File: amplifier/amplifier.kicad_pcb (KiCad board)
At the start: 2 copper layers, 54 x 46.8 mm, 20 parts, among them J1 INPUT, J3 POWER IN, Q1 TIP41, Q2 TIP42, U1 LM833

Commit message: Added HP@DESKTOP-614QREO MINGW64 ~/Documents/KICAD Project (main) $
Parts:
- J2: renamed from SPK OUT
- moved . 1.77 mm to (95.2, 79.5)
- moved . 1.77 mm to (46.8, 79.2)
- moved . 0.79 mm to (95.0, 119.5)
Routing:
- net Net-(D1-K): track 70.9 -> 46.9 mm
- net Net-(J2-Pin_2): track 99.6 -> 100.1 mm
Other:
- board size 54 x 46.8 mm -> 56.7 x 49.5 mm
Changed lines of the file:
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@@
 		(sheetname "/")
 		(sheetfile "amplifier.kicad_sch")
+		(units
+			(unit
+				(name "A")
+				(pins "1" "2")
+			)
+		)
 		(attr through_hole)
 		(duplicate_pad_numbers_are_jumpers no)
@@
 	(footprint "MountingHole:MountingHole_2.2mm_M2_Pad"
 		(layer "F.Cu")
-		(at 95 81.25)
+		(at 95.25 79.5)
 		(descr "Mounting Hole 2.2mm, M2, generated by kicad-footprint-generator mountinghole.py")
 		(tags "mountinghole M2")
@@
 			(at 0 -3.15 0)
 			(layer "B.Cu")
+			(hide yes)
 			(effects
 				(font
@@
 		(sheetname "/")
 		(sheetfile "amplifier.kicad_sch")
+		(units
+			(unit
+				(name "A")
+				(pins "1" "2")
+			)
+		)
 		(attr through_hole)
 		(duplicate_pad_numbers_are_jumpers no)
@@
 			)
 		)
-		(property "Description" ""
+		(property "Description" "Trim-potentiometer, US symbol"
 			(at 0 0 0)
 			(layer "F.Fab")
@@
 		(sheetname "/")
 		(sheetfile "amplifier.kicad_sch")
+		(units
+			(unit
+				(name "A")
+				(pins "1" "3" "2")
+			)
+		)
 		(attr through_hole)
 		(duplicate_pad_numbers_are_jumpers no)
@@
 		(descr "Terminal block Altech AK300, 45Degree (cable under 45degree), 2 pins, pitch 5mm, size 10x12.5mm, drill diameter 1.3mm, pad diameter 3mm, https://www.altechcorp.com/PDFS/PCBMETRC.PDF#page=5, generated with kicad-footprint-generator TerminalBlock_Altech")
 		(tags "THT Terminal block Altech AK300 45Degree pitch 5mm size 10x12.5mm drill 1.3mm pad 3mm")
-		(property "Reference" "SPK OUT"
+		(property "Reference" "J2"
 			(at 2.5 9.5 0)
 			(layer "F.SilkS")
@@
 		(sheetname "/")
 		(sheetfile "amplifier.kicad_sch")
+		(units
+			(unit
+				(name "A")
+				(pins "1" "2")
+			)
+		)
 		(attr through_hole)
 		(duplicate_pad_numbers_are_jumpers no)
@@
 		(sheetname "/")
 		(sheetfile "amplifier.kicad_sch")
+		(units
+			(unit
+				(name "A")
+				(pins "1" "2")
+			)
+		)
 		(attr through_hole)
 		(duplicate_pad_numbers_are_jumpers no)
@@
 		(sheetname "/")
 		(sheetfile "amplifier.kicad_sch")
+		(units
+			(unit
+				(name "A")
+				(pins "1" "2" "3")
+			)
+		)
 		(attr through_hole)
 		(duplicate_pad_numbers_are_jumpers no)
@@
 			(at 0 -3.15 0)
 			(layer "B.Cu")
+			(hide yes)
 			(effects
 				(font
@@
 		(sheetname "/")
 		(sheetfile "amplifier.kicad_sch")
+		(units
+			(unit
+				(name "A")
+				(pins "1" "2")
+			)
+		)
 		(attr through_hole)
 		(duplicate_pad_numbers_are_jumpers no)
@@
 		(sheetname "/")
 		(sheetfile "amplifier.kicad_sch")
+		(units
+			(unit
+				(name "A")
+				(pins "1" "2" "3")
+			)
+		)
 		(attr through_hole)
 		(duplicate_pad_numbers_are_jumpers no)
@@
 	(footprint "MountingHole:MountingHole_2.2mm_M2_Pad"
 		(layer "F.Cu")
-		(at 46.5 81)
+		(at 46.75 79.25)
 		(descr "Mounting Hole 2.2mm, M2, generated by kicad-footprint-generator mountinghole.py")
 		(tags "mountinghole M2")
@@
 			(at 0 -3.15 0)
 			(layer "B.Cu")
+			(hide yes)
 			(effects
 				(font
@@
 	(footprint "MountingHole:MountingHole_2.2mm_M2_Pad"
 		(layer "F.Cu")
-		(at 94.75 120.25)
+		(at 95 119.5)
 		(descr "Mounting Hole 2.2mm, M2, generated by kicad-footprint-generator mountinghole.py")
 		(tags "mountinghole M2")
@@
 			(at 0 -3.15 0)
 			(layer "B.Cu")
+			(hide yes)
 			(effects
 				(font
@@
 		(sheetname "/")
 		(sheetfile "amplifier.kicad_sch")
+		(units
+			(unit
+				(name "A")
+				(pins "1" "2")
+			)
+		)
 		(attr through_hole)
 		(duplicate_pad_numbers_are_jumpers no)
@@
 		(tags "TO-220-3 Vertical RM 2.54mm")
 		(property "Reference" "Q2"
-			(at 2.54 -4.1 90)
+			(at 3 -4.5 90)
 			(layer "F.SilkS")
 			(effects
@@
 		(sheetname "/")
 		(sheetfile "amplifier.kicad_sch")
+		(units
+			(unit
+				(name "A")
+				(pins "1" "2" "3")
+			)
+		)
 		(attr through_hole)
 		(duplicate_pad_numbers_are_jumpers no)
@@
 		(sheetname "/")
 		(sheetfile "amplifier.kicad_sch")
+		(units
+			(unit
+				(name "A")
+				(pins "1" "2")
+			)
+		)
 		(attr through_hole)
 		(duplicate_pad_numbers_are_jumpers no)
@@
 		(sheetname "/")
 		(sheetfile "amplifier.kicad_sch")
+		(units
+			(unit
+				(name "A")
+				(pins "3" "2" "1")
+			)
+			(unit
+				(name "B")
+				(pins "5" "6" "7")
+			)
+			(unit
+				(name "C")
+				(pins "8" "4")
+			)
+		)
 		(attr through_hole)
 		(duplicate_pad_numbers_are_jumpers no)
@@
 		(sheetname "/")
 		(sheetfile "amplifier.kicad_sch")
+		(units
+			(unit
+				(name "A")
+				(pins "1" "2")
+			)
+		)
 		(attr through_hole)
 		(duplicate_pad_numbers_are_jumpers no)
@@
 	)
 	(gr_rect
-		(start 44 76.25)
-		(end 98 123)
+		(start 43.25 75.553072)
+		(end 99.999999 125.089914)
 		(stroke
 			(width 0.05)
@@
 	)
 	(segment
-		(start 56.5 120)
-		(end 53.5 117)
-		(width 1)
+		(start 86.9 110.390173)
+		(end 86.9 101.14)
+		(width 1.2)
 		(layer "F.Cu")
 		(net "Net-(J2-Pin_2)")
 	)
 	(segment
-		(start 89 99.04)
-		(end 83.29 99.04)
-		(width 0.5)
+		(start 83.29 99.04)
+		(end 89 99.04)
+		(width 1.2)
 		(layer "F.Cu")
 		(net "Net-(J2-Pin_2)")
 	)
 	(segment
-		(start 83.29 99.04)
-		(end 82.5 98.25)
-		(width 0.5)
+		(start 86.9 101.14)
+		(end 87.25 100.79)
+		(width 1.2)
 		(layer "F.Cu")
 		(net "Net-(J2-Pin_2)")
 	)
 	(segment
-		(start 68.75 120)
-		(end 56.5 120)
-		(width 1)
+		(start 82.5 98.25)
+		(end 83.29 99.04)
+		(width 1.2)
 		(layer "F.Cu")
 		(net "Net-(J2-Pin_2)")
 	)
 	(segment
-		(start 87.25 110.33)
-		(end 87.25 100.79)
-		(width 0.5)
+		(start 89 112.08)
+		(end 88.589827 112.08)
+		(width 1.2)
 		(layer "F.Cu")
 		(net "Net-(J2-Pin_2)")
 	)
 	(segment
-		(start 89 112.08)
-		(end 87.25 110.33)
-		(width 0.5)
+		(start 56.5 120)
+		(end 68.75 120)
+		(width 1.2)
+		(layer "F.Cu")
+		(net "Net-(J2-Pin_2)")
+	)
+	(segment
+		(start 53.5 117)
+		(end 56.5 120)
+		(width 1.2)
 		(layer "F.Cu")
 		(net "Net-(J2-Pin_2)")
@@
 		(start 87.25 100.79)
 		(end 89 99.04)
-		(width 0.5)
+		(width 1.2)
 		(layer "F.Cu")
 		(net "Net-(J2-Pin_2)")
 	)
 	(segment
-		(start 53.5 117)
-		(end 53.5 113.5)
-		(width 1)
+		(start 88.589827 112.08)
+		(end 86.9 110.390173)
+		(width 1.2)
+		(layer "F.Cu")
+		(net "Net-(J2-Pin_2)")
+	)
+	(segment
+		(start 53.5 113.5)
+		(end 53.5 117)
+		(width 1.2)
 		(layer "F.Cu")
 		(net "Net-(J2-Pin_2)")
@@
 		(end 73.6 88.42)
 		(width 0.2)
+		(locked yes)
 		(layer "B.Cu")
 		(net "+12V")
@@
 	)
 	(segment
-		(start 94.25 91.5)
-		(end 91.5 88.75)
-		(width 0.2)
-		(layer "B.Cu")
-		(net "Net-(D1-K)")
-	)
-	(segment
 		(start 85.5 84.44)
 		(end 82.5 87.44)
@@
 	(segment
 		(start 94.25 92.207107)
-		(end 94.25 101.725)
+		(end 94.25 103.75)
 		(width 1.2)
 		(layer "B.Cu")
@@
 	)
 	(segment
-		(start 91.5 88.75)
-		(end 83.25 88.75)
-		(width 0.2)
-		(layer "B.Cu")
-		(net "Net-(D1-K)")
-	)
-	(segment
-		(start 83.25 88.75)
-		(end 82.5 88)
-		(width 0.2)
-		(layer "B.Cu")
-		(net "Net-(D1-K)")
-	)
-	(segment
 		(start 83.5 89.25)
 		(end 91.292893 89.25)
@@
 		(layer "B.Cu")
 		(net "Net-(D1-K)")
-	)
-	(segment
-		(start 82.5 88)
-		(end 82.5 87.44)
-		(width 0.2)
-		(layer "B.Cu")
-		(net "Net-(D1-K)")
-	)
-	(segment
-		(start 94.25 103.75)
-		(end 94.25 91.5)
-		(width 0.2)
-		(layer "B.Cu")
-		(net "Net-(D1-K)")

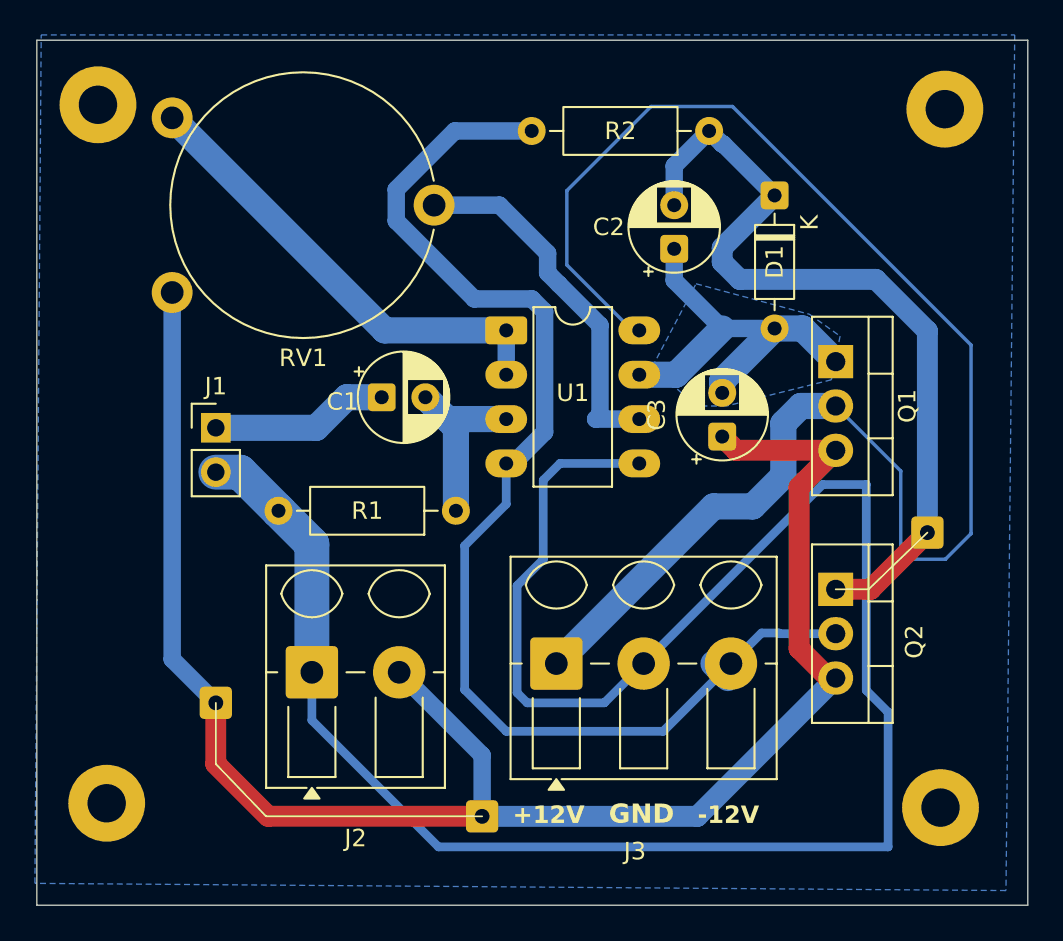
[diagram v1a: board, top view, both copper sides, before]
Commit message: Added amplifier
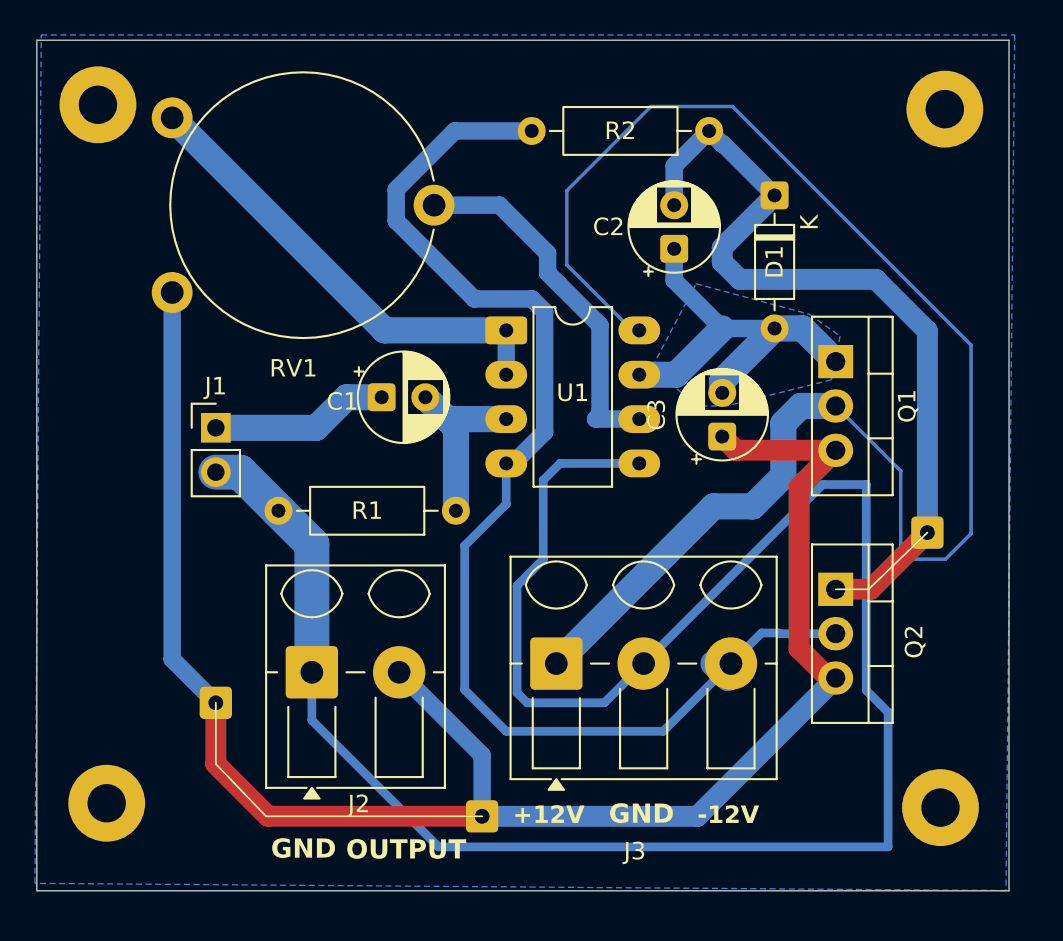
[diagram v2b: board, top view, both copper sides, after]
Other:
- board size 56.7 x 49.5 mm -> 55.7 x 48.7 mm
- board text added: "OUTPUT"
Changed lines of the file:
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@@
 			(crossoutdnponfab yes)
 			(subtractmaskfromsilk no)
-			(outputformat 4)
-			(mirror yes)
+			(outputformat 1)
+			(mirror no)
 			(drillshape 0)
 			(scaleselection 1)
-			(outputdirectory "PDF/")
+			(outputdirectory "Gerber/")
 		)
 	)
@@
 		(tags "Potentiometer vertical Piher PT-15-V15")
 		(property "Reference" "RV1"
-			(at 7.5 3.75 0)
+			(at 6.95 4.35 0)
 			(layer "F.SilkS")
 			(effects
@@
 			)
 		)
-		(property "Description" "Trim-potentiometer, US symbol"
+		(property "Description" ""
 			(at 0 0 0)
 			(layer "F.Fab")
@@
 			)
 		)
-		(property "Sim.Device" "R"
-			(at 0 0 0)
-			(unlocked yes)
-			(layer "F.Fab")
-			(hide yes)
-			(effects
-				(font
-					(size 1 1)
-					(thickness 0.15)
-				)
-			)
-		)
-		(property "Sim.Type" "POT"
-			(at 0 0 0)
-			(unlocked yes)
-			(layer "F.Fab")
-			(hide yes)
-			(effects
-				(font
-					(size 1 1)
-					(thickness 0.15)
-				)
-			)
-		)
-		(property "Sim.Pins" "1=r0 2=wiper 3=r1"
-			(at 0 0 0)
-			(unlocked yes)
-			(layer "F.Fab")
-			(hide yes)
-			(effects
-				(font
-					(size 1 1)
-					(thickness 0.15)
-				)
-			)
-		)
 		(property ki_fp_filters "Potentiometer*")
 		(sheetname "/")
 		(sheetfile "amplifier.kicad_sch")
-		(units
-			(unit
-				(name "A")
-				(pins "1" "3" "2")
-			)
-		)
 		(attr through_hole)
 		(duplicate_pad_numbers_are_jumpers no)
@@
 		)
 		(embedded_fonts no)
-		(model "${KICAD9_3DMODEL_DIR}/Potentiometer_THT.3dshapes/Potentiometer_Piher_PT-15-V15_Vertical.step"
+		(model "C:/Users/HP/Downloads/piher-pt-15v15-1.snapshot.4/Trimmer_Piher_PT-15.step"
 			(offset
-				(xyz 0 0 0)
+				(xyz 8 -5.5 0.5)
 			)
 			(scale
@@
 			)
 			(rotate
-				(xyz 0 0 0)
+				(xyz -90 -0 90)
 			)
 		)
@@
 		(tags "THT Terminal block Altech AK300 45Degree pitch 5mm size 10x12.5mm drill 1.3mm pad 3mm")
 		(property "Reference" "J2"
-			(at 2.5 9.5 0)
+			(at 2.7 7.55 0)
 			(layer "F.SilkS")
 			(effects
@@
 	(gr_rect
 		(start 43.25 75.553072)
-		(end 99.999999 125.089914)
+		(end 98.924424 124.264938)
 		(stroke
 			(width 0.05)
@@
 				(bold yes)
 			)
+			(justify left bottom)
+		)
+	)
+	(gr_text "GND"
+		(at 56.65 122.5 0)
+		(layer "F.SilkS")
+		(effects
+			(font
+				(size 1.1 1.1)
+				(thickness 0.275)
+				(bold yes)
+			)
+			(justify left bottom)
+		)
+	)
+	(gr_text "OUTPUT"
+		(at 60.95 122.55 0)
+		(layer "F.SilkS")
+		(effects
+			(font
+				(size 1.1 1.1)
+				(thickness 0.275)
+				(bold yes)
+			)
